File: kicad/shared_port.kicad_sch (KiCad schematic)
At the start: 30 parts, among them J1 Keyboard (2x10 box), J2 SNES pad, J3 SNES pad, J4 SD (SPI), J5 PS/2 kbd + mouse, U37 SN74HC574N, U38 ATF22V10C-7PX, U39 SN74F541N

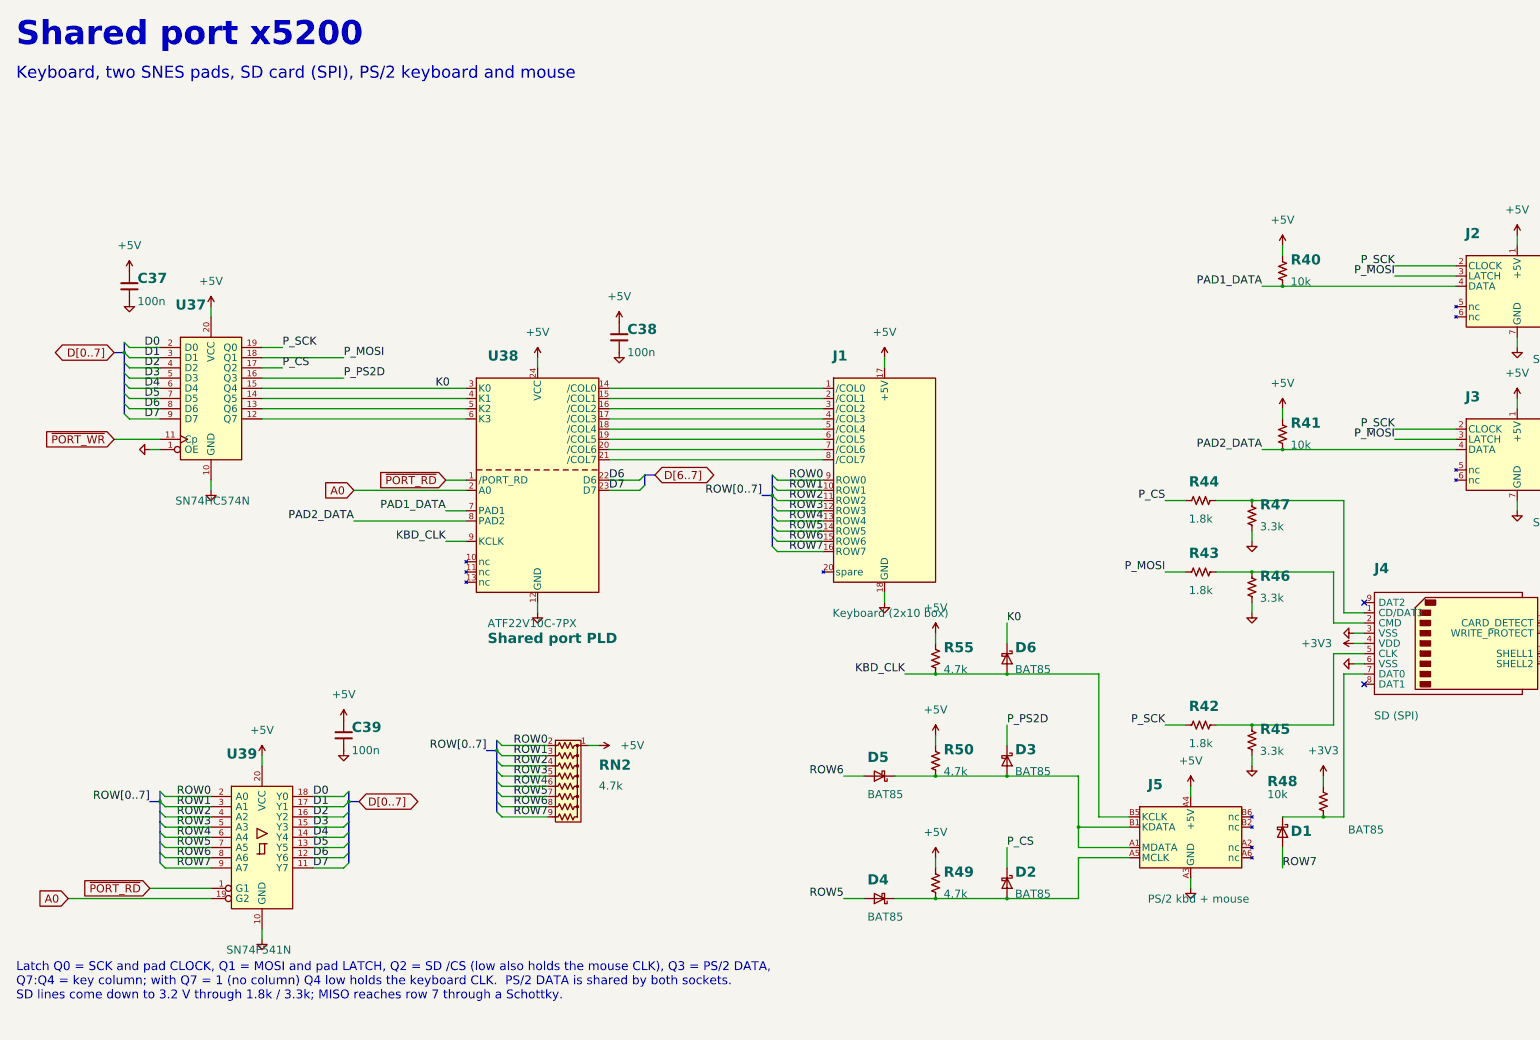
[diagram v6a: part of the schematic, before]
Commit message: Carry the PS/2 receiver PLD and the dropped matrix keyboard through the design
The matrix keyboard (U37, U39, J1, RN2, the keyboard board) is gone and the
PS/2 receiver PLD U42 (ATF22V10_PS2.pld rev 02) is added everywhere except
the hand-edited board layout:

- Drivers: receiver-based kbd_scan / mouse_poll / ps2_poll, PS2_LSN listened
  device, ps2_pause waits for a half-received mouse byte and holds the line
  at least 100 us; pad_read frees the mouse clock only briefly.
- Simulator: PS/2 keyboard and mouse models with abort/resend; tests pass.
- Bring-up ROM polls the PS/2 keyboard; BRINGUP.md step 18 rewritten.
- FPGA: port_pld rev 04, new ps2_pld, basys_top wired to both, matrix gone.
- Schematic: shared port sheet redrawn (U38, U42, D1/D4/D5/D19, R60),
  keyboard project, key switch footprints and header removed, C42 -> C47,
  PDFs and I/O PNG regenerated (netlist and ERC clean).
- BOM: keyboard board removed, U42 and C42 added; main board $184.77.
- Docs: IO, CHIPS, PLD_USAGE, LIBRARY, MENU, SCHEMATIC_PLAN, KITTING,
  EXPANSION, ROM, README, kicad README; dated notes in KIT_PRICING and CASE
  (keyboard kit and keyboard bay are moot, re-cost and case rethink pending).
- Block diagram regenerated (33 chips).

Co-Authored-By: Claude Fable 5.1 <noreply@anthropic.com>
Claude-Session: https://claude.ai/code/session_01QpoMmygNy6VSnJkmoq279r
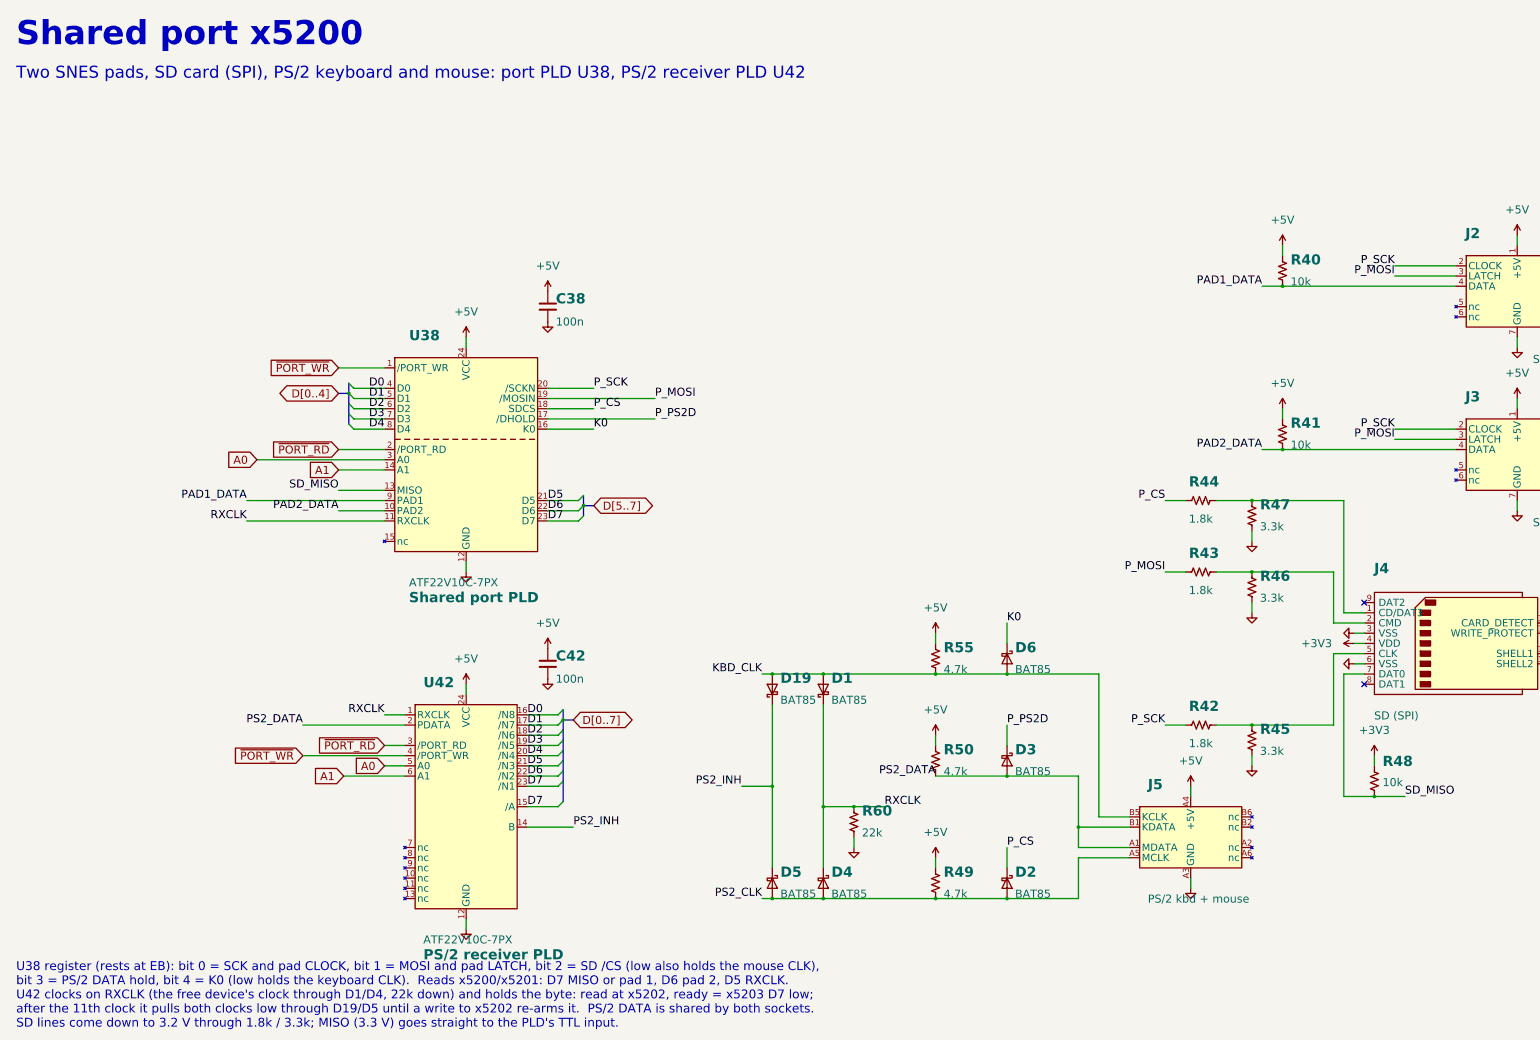
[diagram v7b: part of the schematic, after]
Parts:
- removed C37, C39: 100n, Capacitor_THT:C_Disc_D5.0mm_W2.5mm_P5.00mm, symbol placard_std:C
- removed J1: Keyboard (2x10 box), Connector_IDC:IDC-Header_2x10_P2.54mm_Vertical, symbol placard_parts:Keyboard_Header
- removed RN2: 4.7k, Resistor_THT:R_Array_SIP9, symbol placard_std:R_Network08_US
- removed U37: SN74HC574N, placard:DIP-20_W7.62mm_Socket_Puller, symbol placard_std:74LS574
- removed U39: SN74F541N, placard:DIP-20_W7.62mm_Socket_Puller, symbol placard_std:74LS541
- added C42: 100n, Capacitor_THT:C_Disc_D5.0mm_W2.5mm_P5.00mm, symbol placard_std:C
- added D19: BAT85, Diode_THT:D_DO-35_SOD27_P7.62mm_Horizontal, symbol placard_std:D_Schottky
- added R60: 22k, placard:R_Axial_DIN0207_L6.3mm_D2.5mm_P10.16mm_Horizontal_Value, symbol placard_std:R_US
- added U42: ATF22V10C-7PX, placard:DIP-24_W7.62mm_Socket_Puller, symbol placard:ATF22V10C_PS2
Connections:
- net ROW5 is gone; now on net PS2_CLK: D4.2 (A)
- net ROW6 is gone; now on net PS2_CLK: D5.2 (A)
- net ROW7 is gone; now on net KBD_CLK: D1.2 (A)
- net +5V: now also C42.1, U42.24 (VCC)
- net A0: now also U38.3 (A0), U42.5 (A0); no longer U38.2 (A0)
- net D0: now also U38.4 (D0), U42.16 (/N8)
- net D1: now also U38.5 (D1), U42.17 (/N7)
- net D2: now also U38.6 (D2), U42.18 (/N6)
- net D3: now also U38.7 (D3), U42.19 (/N5)
- net D4: now also U38.8 (D4), U42.20 (/N4)
- net D5: now also U38.21 (D5), U42.21 (/N3)
- net D6: now also U42.22 (/N2)
- net D7: now also U42.15 (/A), U42.23 (/N1)
- net GND: now also C42.2, R60.2, U42.12 (GND)
- net K0: now also U38.16 (K0); no longer U38.3 (K0)
- net KBD_CLK: now also D19.2 (A); no longer U38.9 (KCLK)
- net PAD1_DATA: now also U38.9 (PAD1); no longer U38.7 (PAD1)
- net PAD2_DATA: now also U38.10 (PAD2); no longer U38.8 (PAD2)
- net P_CS: now also U38.18 (SDCS)
- net P_MOSI: now also U38.19 (/MOSIN)
- net P_PS2D: now also U38.17 (/DHOLD)
- net P_SCK: now also U38.20 (/SCKN)
- net ~{PORT_RD}: now also U38.2 (/PORT_RD), U42.3 (/PORT_RD); no longer U38.1 (/PORT_RD)
- net ~{PORT_WR}: now also U38.1 (/PORT_WR), U42.4 (/PORT_WR)
- net PS2_DATA: now reaches D3.2 (A), J5.A1 (MDATA), J5.B1 (KDATA), R50.2
- net PS2_DATA: now also U42.2 (PDATA); no longer D5.1 (K)
- net SD_MISO: now reaches J4.7 (DAT0), R48.2
- net SD_MISO: now also U38.13 (MISO); no longer D1.1 (K)
- net RXCLK: now reaches U38.11 (RXCLK)
- net RXCLK: now also D1.1 (K), D4.1 (K), R60.1, U42.1 (RXCLK)
- net A1: now reaches U38.14 (A1)
- net A1: now also U42.6 (A1)
- net PS2_CLK: now reaches D2.2 (A), J5.A5 (MCLK), R49.2
- net PS2_CLK: no longer D4.1 (K)
- new net PS2_INH: D19.1 (K), D5.1 (K), U42.14 (B)
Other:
- note added: "SD lines come down to 3.2 V through 1.8k / 3.3k; MISO (3.3 V) goes straight to the PLD's TTL input."
- note added: "Two SNES pads, SD card (SPI), PS/2 keyboard and mouse: port PLD U38, PS/2 receiver PLD U42"
- note added: "U38 register (rests at EB): bit 0 = SCK and pad CLOCK, bit 1 = MOSI and pad LATCH, bit 2 = SD /CS (low also holds the mouse CLK),"
- note added: "U42 clocks on RXCLK (the free device's clock through D1/D4, 22k down) and holds the byte: read at x5202, ready = x5203 D7 low;"
- note added: "after the 11th clock it pulls both clocks low through D19/D5 until a write to x5202 re-arms it. PS/2 DATA is shared by both sockets."
- note added: "bit 3 = PS/2 DATA hold, bit 4 = K0 (low holds the keyboard CLK). Reads x5200/x5201: D7 MISO or pad 1, D6 pad 2, D5 RXCLK."
- note removed: "Keyboard, two SNES pads, SD card (SPI), PS/2 keyboard and mouse"
- note removed: "Latch Q0 = SCK and pad CLOCK, Q1 = MOSI and pad LATCH, Q2 = SD /CS (low also holds the mouse CLK), Q3 = PS/2 DATA,"
- note removed: "Q7:Q4 = key column; with Q7 = 1 (no column) Q4 low holds the keyboard CLK. PS/2 DATA is shared by both sockets."
- note removed: "SD lines come down to 3.2 V through 1.8k / 3.3k; MISO reaches row 7 through a Schottky."
- moved on the sheet: C38, D1, D4, D5, R48

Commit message: Rename the mouse clock net PS2_CLK to MOUS_CLK
Matches KBD_CLK for the keyboard socket. PS2_DATA stays: it is shared
by both sockets. Schematic regenerated (also fixes the stale U1-U40
title-block comment), PDF and I/O PNG re-rendered, IO.md and PLD
comments updated. The Basys 3 PS2_CLK port in the FPGA top level is the
dev board's own pin and is unchanged.

Co-Authored-By: Claude Opus 5.5 (1M context) <noreply@anthropic.com>
Claude-Session: https://claude.ai/code/session_01KP4BubMKupRWajK8nHpymc
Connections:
- net PS2_CLK renamed MOUS_CLK
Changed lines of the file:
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@@
 (kicad_sch (version 20230121) (generator eeschema)
   (paper "A3")
-  (title_block (title "Placard: Shared port") (date "2026-10-25") (rev "1") (company "Placard computer") (comment 1 "Generated by src/scripts/gen_kicad_schematic.py; plan in docs/SCHEMATIC_PLAN.md") (comment 2 "Chip numbers U1-U40 = docs/CHIPS.md; decoupling Cn goes with Un"))
+  (title_block (title "Placard: Shared port") (date "2026-10-25") (rev "1") (company "Placard computer") (comment 1 "Generated by src/scripts/gen_kicad_schematic.py; plan in docs/SCHEMATIC_PLAN.md") (comment 2 "Chip numbers U1-U42 = docs/CHIPS.md; decoupling Cn goes with Un"))
   (text "Shared port x5200" (at 15 22 0) (effects (font (size 6 6) bold) (justify left bottom)))
   (text "Two SNES pads, SD card (SPI), PS/2 keyboard and mouse: port PLD U38, PS/2 receiver PLD U42" (at 15 30 0) (effects (font (size 3 3)) (justify left bottom)))
@@
   (label "KBD_CLK" (at 200.66 177.8 180) (fields_autoplaced) (effects (font (size 2 2)) (justify right bottom)))
   (label "PS2_DATA" (at 243.84 203.2 180) (fields_autoplaced) (effects (font (size 2 2)) (justify right bottom)))
-  (label "PS2_CLK" (at 200.66 233.68 180) (fields_autoplaced) (effects (font (size 2 2)) (justify right bottom)))
+  (label "MOUS_CLK" (at 200.66 233.68 180) (fields_autoplaced) (effects (font (size 2 2)) (justify right bottom)))
   (label "PS2_INH" (at 195.58 205.74 180) (fields_autoplaced) (effects (font (size 2 2)) (justify right bottom)))
   (label "RXCLK" (at 231.14 210.82 0) (fields_autoplaced) (effects (font (size 2 2)) (justify left bottom)))
